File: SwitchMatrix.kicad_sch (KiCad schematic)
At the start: 134 parts, among them K1 Kailh Hotswap Socket, K10 Kailh Hotswap Socket, K11 Kailh Hotswap Socket, K12 Kailh Hotswap Socket, K13 Kailh Hotswap Socket, K14 Kailh Hotswap Socket, K15 Kailh Hotswap Socket, K16 Kailh Hotswap Socket, K17 Kailh Hotswap Socket, K18 Kailh Hotswap Socket, K19 Kailh Hotswap Socket, K2 Kailh Hotswap Socket, K20 Kailh Hotswap Socket, K21 Kailh Hotswap Socket, K22 Kailh Hotswap Socket, K23 Kailh Hotswap Socket, K24 Kailh Hotswap Socket, K25 Kailh Hotswap Socket, K26 Kailh Hotswap Socket, K27 Kailh Hotswap Socket, K28 Kailh Hotswap Socket, K29 Kailh Hotswap Socket, K3 Kailh Hotswap Socket, K30 Kailh Hotswap Socket, K31 Kailh Hotswap Socket, K32 Kailh Hotswap Socket, K33 Kailh Hotswap Socket, K34 Kailh Hotswap Socket, K35 Kailh Hotswap Socket, K36 Kailh Hotswap Socket, K37 Kailh Hotswap Socket, K38 Kailh Hotswap Socket, K39 Kailh Hotswap Socket, K4 Kailh Hotswap Socket, K40 Kailh Hotswap Socket, K41 Kailh Hotswap Socket, K42 Kailh Hotswap Socket, K43 Kailh Hotswap Socket, K44 Kailh Hotswap Socket, K45 Kailh Hotswap Socket, K46 Kailh Hotswap Socket, K47 Kailh Hotswap Socket, K48 Kailh Hotswap Socket, K49 Kailh Hotswap Socket, K5 Kailh Hotswap Socket, K50 Kailh Hotswap Socket, K51 Kailh Hotswap Socket, K52 Kailh Hotswap Socket, K53 Kailh Hotswap Socket, K54 Kailh Hotswap Socket, K55 Kailh Hotswap Socket, K56 Kailh Hotswap Socket, K57 Kailh Hotswap Socket, K58 Kailh Hotswap Socket, K59 Kailh Hotswap Socket, K6 Kailh Hotswap Socket, K60 Kailh Hotswap Socket, K61 Kailh Hotswap Socket, K62 Kailh Hotswap Socket, K63 Kailh Hotswap Socket, K64 Kailh Hotswap Socket, K7 Kailh Hotswap Socket, K8 Kailh Hotswap Socket, K9 Kailh Hotswap Socket

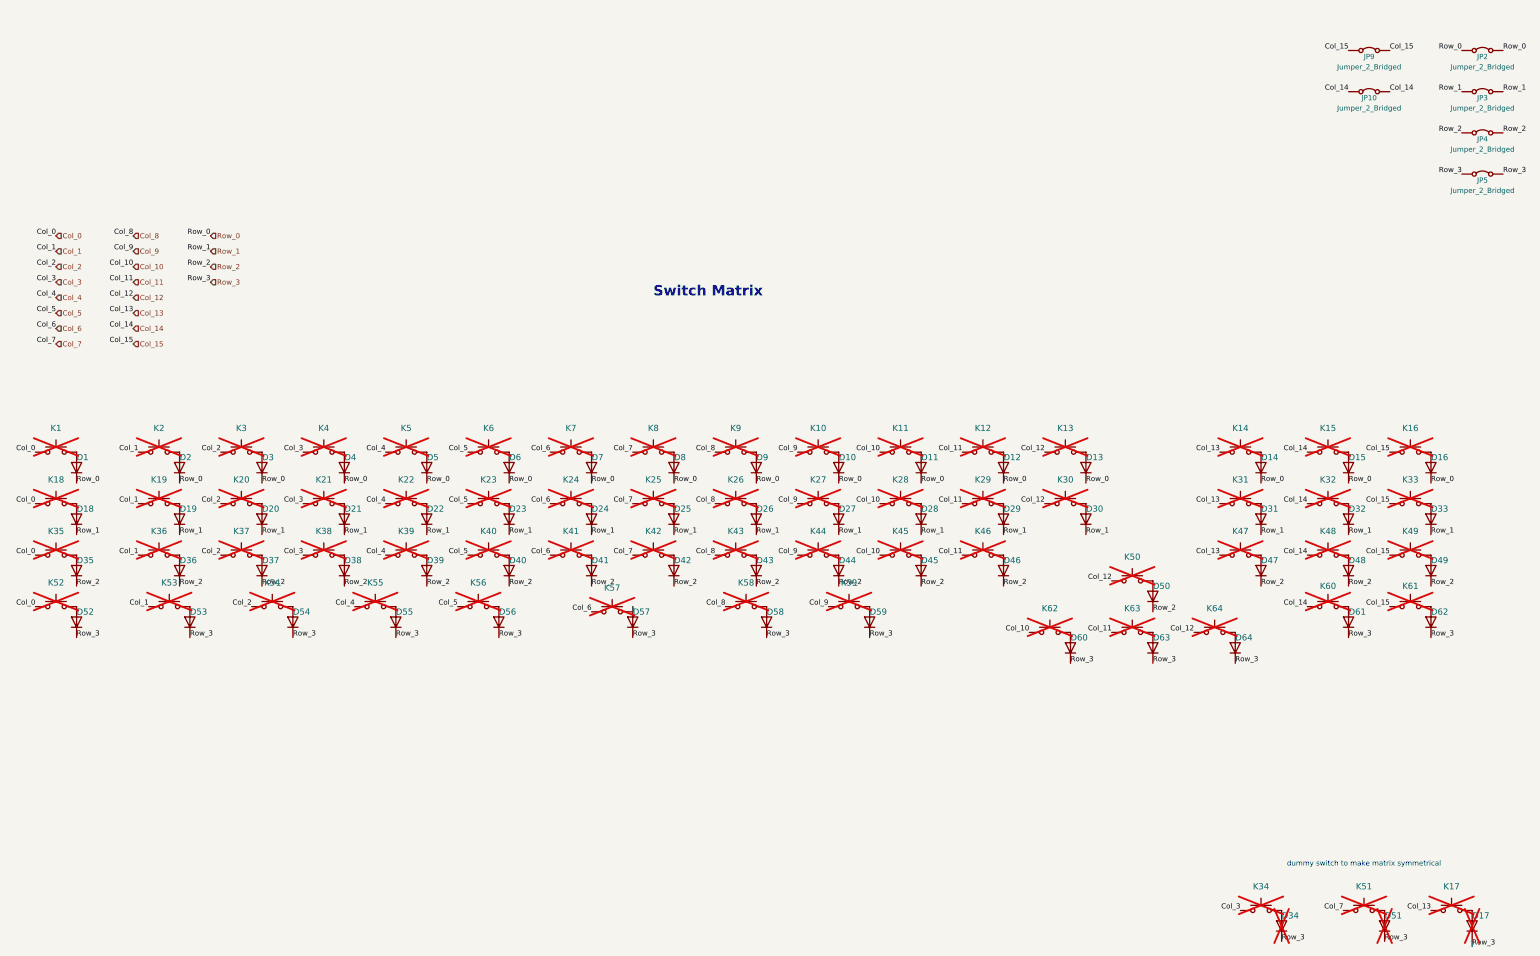
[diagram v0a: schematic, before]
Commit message: usb changes for high power (leds)
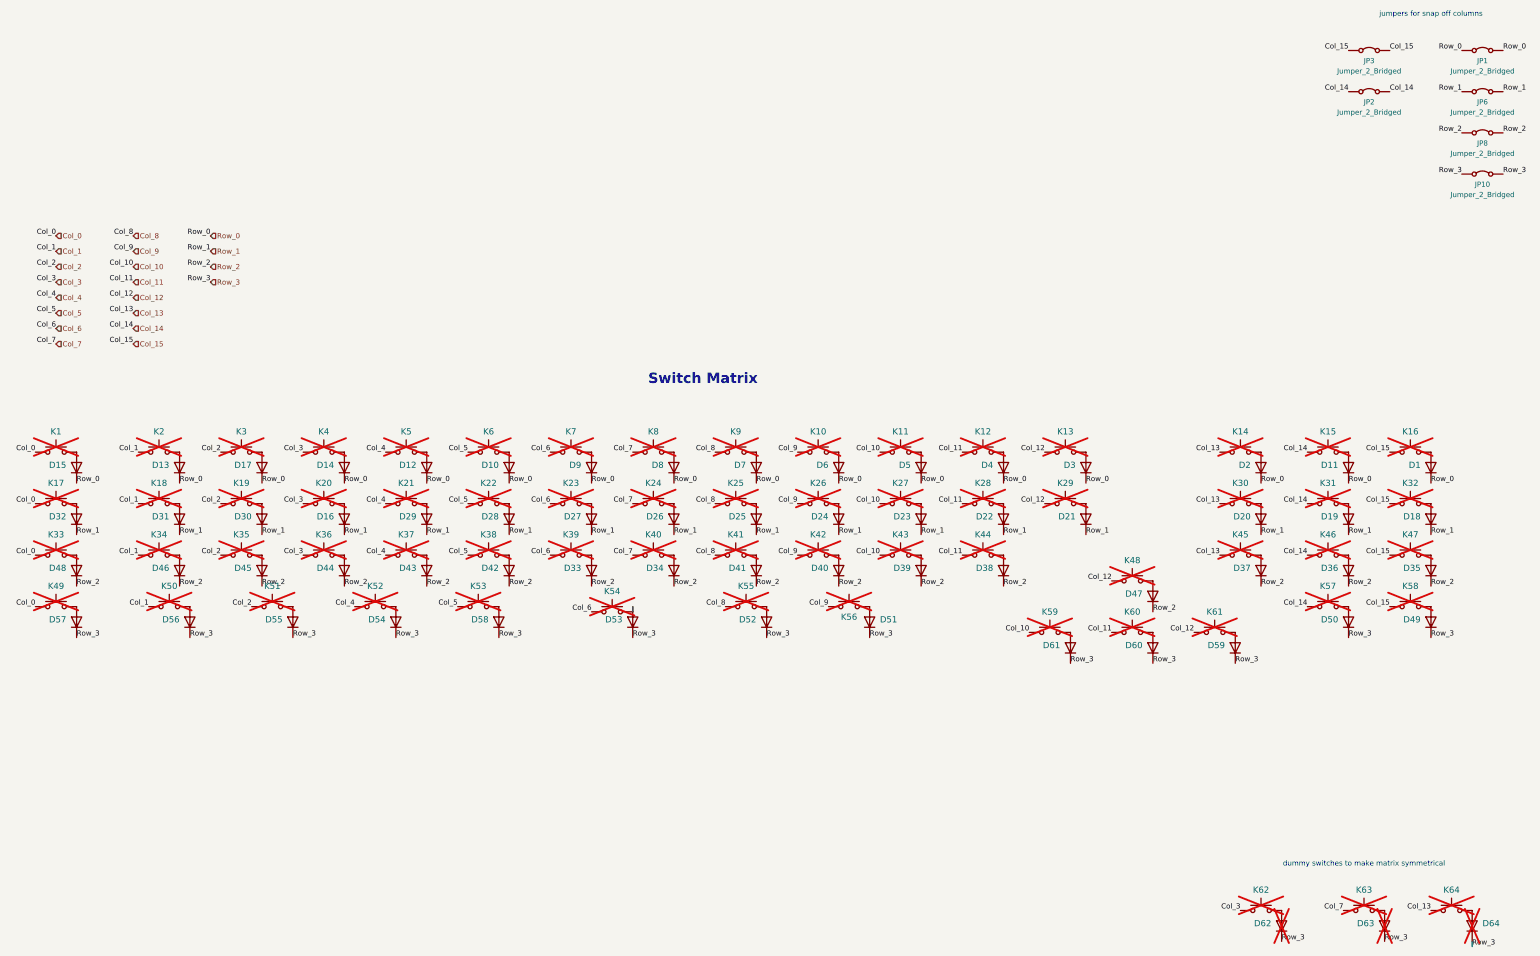
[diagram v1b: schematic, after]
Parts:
- renumbered D16 to D1, D6 to D10, D15 to D11, D5 to D12, D2 to D13, D4 to D14, D1 to D15, D21 to D16, D3 to D17, D33 to D18, D32 to D19, D14 to D2, D31 to D20, D30 to D21, D29 to D22, D28 to D23, D27 to D24, D26 to D25, D25 to D26, D24 to D27, D23 to D28, D22 to D29, D13 to D3, D20 to D30, D19 to D31, D18 to D32, D41 to D33, D42 to D34, D49 to D35, D48 to D36, D47 to D37, D46 to D38, D45 to D39, D12 to D4, D44 to D40, D43 to D41, D40 to D42, D39 to D43, D38 to D44, D37 to D45, D36 to D46, D50 to D47, D35 to D48, D62 to D49, D11 to D5, D61 to D50, D59 to D51, D58 to D52, D57 to D53, D55 to D54, D54 to D55, D53 to D56, D52 to D57, D56 to D58, D64 to D59, D10 to D6, D63 to D60, D60 to D61, D34 to D62, D51 to D63, D17 to D64, D9 to D7, D7 to D9, JP2 to JP1, JP5 to JP10, JP10 to JP2, JP9 to JP3, JP3 to JP6, JP4 to JP8, K18 to K17, K19 to K18, K20 to K19, K21 to K20, K22 to K21, K23 to K22, K24 to K23, K25 to K24, K26 to K25, K27 to K26, K28 to K27, K29 to K28, K30 to K29, K31 to K30, K32 to K31, K33 to K32, K35 to K33, K36 to K34, K37 to K35, K38 to K36, K39 to K37, K40 to K38, K41 to K39, K42 to K40, K43 to K41, K44 to K42, K45 to K43, K46 to K44, K47 to K45, K48 to K46, K49 to K47, K50 to K48, K52 to K49, K53 to K50, K54 to K51, K55 to K52, K56 to K53, K57 to K54, K58 to K55, K59 to K56, K60 to K57, K61 to K58, K62 to K59, K63 to K60, K64 to K61, K34 to K62, K51 to K63, K17 to K64
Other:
- note added: "dummy switches to make matrix symmetrical"
- note added: "jumpers for snap off columns"
- note removed: "dummy switch to make matrix symmetrical"

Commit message: bulk cap and level shifter (still need to lay out)
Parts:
- D1, D10, D11, D12, D13, D14, D15, D16, D17, D18, D19, D2, D20, D21, D22, D23, D24, D25, D26, D27, D28, D29, D3, D30, D31, D32, D33, D34, D35, D36, D37, D38, D39, D4, D40, D41, D42, D43, D44, D45, D46, D47, D48, D49, D5, D50, D51, D52, D53, D54, D55, D56, D57, D58, D59, D6, D60, D61, D7, D8, D9: LCSC C2828417 -> C81598; MPN (none) -> 1N4148W; Manufacturer 1N4148W -> ST(Semtech)
- D62, D63, D64: MPN (none) -> DNP
- JP1, JP10, JP2, JP3, JP6, JP8: MPN (none) -> DNP; now not fitted
- K1, K10, K11, K12, K13, K14, K15, K16, K17, K18, K19, K2, K20, K21, K22, K23, K24, K25, K26, K27, K28, K29, K3, K30, K31, K32, K33, K34, K35, K36, K37, K38, K39, K4, K40, K41, K42, K43, K44, K45, K46, K47, K48, K5, K57, K58, K59, K6, K60, K61, K62, K63, K64, K7, K8, K9: footprint PCM_Switch_Keyboard_Hotswap_Kailh:SW_Hotswap_Kailh_MX_1.00u -> PCM_Switch_Keyboard_Hotswap_Kailh:SW_Hotswap_Kailh_MX_Plated; MPN 4958 -> 4958
- K49, K50, K51, K52, K53, K55, K56: footprint PCM_Switch_Keyboard_Hotswap_Kailh:SW_Hotswap_Kailh_MX_1.25u -> PCM_Switch_Keyboard_Hotswap_Kailh:SW_Hotswap_Kailh_MX_Plated_1.25u; MPN 4958 -> 4958
- K54: footprint PCM_Switch_Keyboard_Hotswap_Kailh:SW_Hotswap_Kailh_MX_2.00u -> PCM_Switch_Keyboard_Hotswap_Kailh:SW_Hotswap_Kailh_MX_Plated_2.00u; MPN 4958 -> 4958

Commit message: add debug led, make bulk caps smaller, export plate and bottom for rudimentary case
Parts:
- D1, D10, D11, D12, D13, D14, D15, D16, D17, D18, D19, D2, D20, D21, D22, D23, D24, D25, D26, D27, D28, D29, D3, D30, D31, D32, D33, D34, D35, D36, D37, D38, D39, D4, D40, D41, D42, D43, D44, D45, D46, D47, D48, D49, D5, D50, D51, D52, D53, D54, D55, D56, D57, D58, D59, D6, D60, D61, D7, D8, D9: Manufacturer ST(Semtech) -> ST(Semtech)
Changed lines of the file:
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@@
 			)
 		)
-		(property "Manufacturer" " ST(Semtech)"
+		(property "Manufacturer" "ST(Semtech)"
 			(at 38.1 153.67 0)
 			(effects
@@
 			)
 		)
-		(property "Manufacturer" " ST(Semtech)"
+		(property "Manufacturer" "ST(Semtech)"
 			(at 372.11 128.27 0)
 			(effects
@@
 			)
 		)
-		(property "Manufacturer" " ST(Semtech)"
+		(property "Manufacturer" "ST(Semtech)"
 			(at 372.11 166.37 0)
 			(effects
@@
 			)
 		)
-		(property "Manufacturer" " ST(Semtech)"
+		(property "Manufacturer" "ST(Semtech)"
 			(at 233.68 166.37 0)
 			(effects
@@
 			)
 		)
-		(property "Manufacturer" " ST(Semtech)"
+		(property "Manufacturer" "ST(Semtech)"
 			(at 104.14 153.67 0)
 			(effects
@@
 			)
 		)
-		(property "Manufacturer" " ST(Semtech)"
+		(property "Manufacturer" "ST(Semtech)"
 			(at 303.53 160.02 0)
 			(effects
@@
 			)
 		)
-		(property "Manufacturer" " ST(Semtech)"
+		(property "Manufacturer" "ST(Semtech)"
 			(at 63.5 153.67 0)
 			(effects
@@
 			)
 		)
-		(property "Manufacturer" " ST(Semtech)"
+		(property "Manufacturer" "ST(Semtech)"
 			(at 104.14 140.97 0)
 			(effects
@@
 			)
 		)
-		(property "Manufacturer" " ST(Semtech)"
+		(property "Manufacturer" "ST(Semtech)"
 			(at 226.06 153.67 0)
 			(effects
@@
 			)
 		)
-		(property "Manufacturer" " ST(Semtech)"
+		(property "Manufacturer" "ST(Semtech)"
 			(at 205.74 153.67 0)
 			(effects
@@
 			)
 		)
-		(property "Manufacturer" " ST(Semtech)"
+		(property "Manufacturer" "ST(Semtech)"
 			(at 351.79 140.97 0)
 			(effects
@@
 			)
 		)
-		(property "Manufacturer" " ST(Semtech)"
+		(property "Manufacturer" "ST(Semtech)"
 			(at 124.46 140.97 0)
 			(effects
@@
 			)
 		)
-		(property "Manufacturer" " ST(Semtech)"
+		(property "Manufacturer" "ST(Semtech)"
 			(at 246.38 128.27 0)
 			(effects
@@
 			)
 		)
-		(property "Manufacturer" " ST(Semtech)"
+		(property "Manufacturer" "ST(Semtech)"
 			(at 63.5 128.27 0)
 			(effects
@@
 			)
 		)
-		(property "Manufacturer" " ST(Semtech)"
+		(property "Manufacturer" "ST(Semtech)"
 			(at 144.78 128.27 0)
 			(effects
@@
 			)
 		)
-		(property "Manufacturer" " ST(Semtech)"
+		(property "Manufacturer" "ST(Semtech)"
 			(at 83.82 140.97 0)
 			(effects
@@
 			)
 		)
-		(property "Manufacturer" " ST(Semtech)"
+		(property "Manufacturer" "ST(Semtech)"
 			(at 205.74 140.97 0)
 			(effects
@@
 			)
 		)
-		(property "Manufacturer" " ST(Semtech)"
+		(property "Manufacturer" "ST(Semtech)"
 			(at 38.1 140.97 0)
 			(effects
@@
 			)
 		)
-		(property "Manufacturer" " ST(Semtech)"
+		(property "Manufacturer" "ST(Semtech)"
 			(at 246.38 140.97 0)
 			(effects
@@
 			)
 		)
-		(property "Manufacturer" " ST(Semtech)"
+		(property "Manufacturer" "ST(Semtech)"
 			(at 124.46 128.27 0)
 			(effects
@@
 			)
 		)
-		(property "Manufacturer" " ST(Semtech)"
+		(property "Manufacturer" "ST(Semtech)"
 			(at 83.82 153.67 0)
 			(effects
@@
 			)
 		)
-		(property "Manufacturer" " ST(Semtech)"
+		(property "Manufacturer" "ST(Semtech)"
 			(at 287.02 128.27 0)
 			(effects
@@
 			)
 		)
-		(property "Manufacturer" " ST(Semtech)"
+		(property "Manufacturer" "ST(Semtech)"
 			(at 66.04 166.37 0)
 			(effects
@@
 			)
 		)
-		(property "Manufacturer" " ST(Semtech)"
+		(property "Manufacturer" "ST(Semtech)"
 			(at 185.42 128.27 0)
 			(effects
@@
 			)
 		)
-		(property "Manufacturer" " ST(Semtech)"
+		(property "Manufacturer" "ST(Semtech)"
 			(at 175.26 166.37 0)
 			(effects
@@
 			)
 		)
-		(property "Manufacturer" " ST(Semtech)"
+		(property "Manufacturer" "ST(Semtech)"
 			(at 116.84 166.37 0)
 			(effects
@@
 			)
 		)
-		(property "Manufacturer" " ST(Semtech)"
+		(property "Manufacturer" "ST(Semtech)"
 			(at 165.1 153.67 0)
 			(effects
@@
 			)
 		)
-		(property "Manufacturer" " ST(Semtech)"
+		(property "Manufacturer" "ST(Semtech)"
 			(at 226.06 140.97 0)
 			(effects
@@
 			)
 		)
-		(property "Manufacturer" " ST(Semtech)"
+		(property "Manufacturer" "ST(Semtech)"
 			(at 91.44 166.37 0)
 			(effects
@@
 			)
 		)
-		(property "Manufacturer" " ST(Semtech)"
+		(property "Manufacturer" "ST(Semtech)"
 			(at 372.11 153.67 0)
 			(effects
@@
 			)
 		)
-		(property "Manufacturer" " ST(Semtech)"
+		(property "Manufacturer" "ST(Semtech)"
 			(at 104.14 128.27 0)
 			(effects
@@
 			)
 		)
-		(property "Manufacturer" " ST(Semtech)"
+		(property "Manufacturer" "ST(Semtech)"
 			(at 351.79 153.67 0)
 			(effects
@@
 			)
 		)
-		(property "Manufacturer" " ST(Semtech)"
+		(property "Manufacturer" "ST(Semtech)"
 			(at 144.78 140.97 0)
 			(effects
@@
 			)
 		)
-		(property "Manufacturer" " ST(Semtech)"
+		(property "Manufacturer" "ST(Semtech)"
 			(at 165.1 128.27 0)
 			(effects
@@
 			)
 		)
-		(property "Manufacturer" " ST(Semtech)"
+		(property "Manufacturer" "ST(Semtech)"
 			(at 208.28 166.37 0)
 			(effects
@@
 			)
 		)
-		(property "Manufacturer" " ST(Semtech)"
+		(property "Manufacturer" "ST(Semtech)"
 			(at 246.38 153.67 0)
 			(effects
@@
 			)
 		)
-		(property "Manufacturer" " ST(Semtech)"
+		(property "Manufacturer" "ST(Semtech)"
 			(at 266.7 140.97 0)
 			(effects
@@
 			)
 		)
-		(property "Manufacturer" " ST(Semtech)"
+		(property "Manufacturer" "ST(Semtech)"
 			(at 330.2 128.27 0)
 			(effects
@@
 			)
 		)
-		(property "Manufacturer" " ST(Semtech)"
+		(property "Manufacturer" "ST(Semtech)"
 			(at 205.74 128.27 0)
 			(effects
@@
 			)
 		)
-		(property "Manufacturer" " ST(Semtech)"
+		(property "Manufacturer" "ST(Semtech)"
 			(at 287.02 140.97 0)
 			(effects
@@
 			)
 		)
-		(property "Manufacturer" " ST(Semtech)"
+		(property "Manufacturer" "ST(Semtech)"
 			(at 38.1 128.27 0)
 			(effects
@@
 			)
 		)
-		(property "Manufacturer" " ST(Semtech)"
+		(property "Manufacturer" "ST(Semtech)"
 			(at 283.21 172.72 0)
 			(effects
@@
 			)
 		)
-		(property "Manufacturer" " ST(Semtech)"
+		(property "Manufacturer" "ST(Semtech)"
 			(at 266.7 128.27 0)
 			(effects
@@
 			)
 		)
-		(property "Manufacturer" " ST(Semtech)"
+		(property "Manufacturer" "ST(Semtech)"
 			(at 303.53 172.72 0)
 			(effects
@@
 			)
 		)
-		(property "Manufacturer" " ST(Semtech)"
+		(property "Manufacturer" "ST(Semtech)"
 			(at 63.5 140.97 0)
 			(effects
@@
 			)
 		)
-		(property "Manufacturer" " ST(Semtech)"
+		(property "Manufacturer" "ST(Semtech)"
 			(at 226.06 128.27 0)
 			(effects
@@
 			)
 		)
-		(property "Manufacturer" " ST(Semtech)"
+		(property "Manufacturer" "ST(Semtech)"
 			(at 351.79 128.27 0)
 			(effects
@@
 			)
 		)
-		(property "Manufacturer" " ST(Semtech)"
+		(property "Manufacturer" "ST(Semtech)"
 			(at 330.2 140.97 0)
 			(effects
@@
 			)
 		)
-		(property "Manufacturer" " ST(Semtech)"
+		(property "Manufacturer" "ST(Semtech)"
 			(at 330.2 153.67 0)
 			(effects
@@
 			)
 		)
-		(property "Manufacturer" " ST(Semtech)"
+		(property "Manufacturer" "ST(Semtech)"
 			(at 38.1 166.37 0)
 			(effects
@@
 			)
 		)
-		(property "Manufacturer" " ST(Semtech)"
+		(property "Manufacturer" "ST(Semtech)"
 			(at 144.78 153.67 0)
 			(effects
@@
 			)
 		)
-		(property "Manufacturer" " ST(Semtech)"
+		(property "Manufacturer" "ST(Semtech)"
 			(at 185.42 153.67 0)
 			(effects
@@
 			)
 		)
-		(property "Manufacturer" " ST(Semtech)"
+		(property "Manufacturer" "ST(Semtech)"
 			(at 372.11 140.97 0)
 			(effects
@@
 			)
 		)
-		(property "Manufacturer" " ST(Semtech)"
+		(property "Manufacturer" "ST(Semtech)"
 			(at 124.46 153.67 0)
 			(effects
@@
 			)
 		)
-		(property "Manufacturer" " ST(Semtech)"
+		(property "Manufacturer" "ST(Semtech)"
 			(at 266.7 153.67 0)
 			(effects
@@
 			)
 		)
-		(property "Manufacturer" " ST(Semtech)"
+		(property "Manufacturer" "ST(Semtech)"
 			(at 351.79 166.37 0)
 			(effects
@@
 			)
 		)
-		(property "Manufacturer" " ST(Semtech)"
+		(property "Manufacturer" "ST(Semtech)"
 			(at 142.24 166.37 0)
 			(effects
@@
 			)
 		)
-		(property "Manufacturer" " ST(Semtech)"
+		(property "Manufacturer" "ST(Semtech)"
 			(at 83.82 128.27 0)
 			(effects
@@
 			)
 		)
-		(property "Manufacturer" " ST(Semtech)"
+		(property "Manufacturer" "ST(Semtech)"
 			(at 185.42 140.97 0)
 			(effects
@@
 			)
 		)
-		(property "Manufacturer" " ST(Semtech)"
+		(property "Manufacturer" "ST(Semtech)"
 			(at 165.1 140.97 0)
 			(effects
@@
 			)
 		)
-		(property "Manufacturer" " ST(Semtech)"
+		(property "Manufacturer" "ST(Semtech)"
 			(at 323.85 172.72 0)
 			(effects

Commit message: enlarge mounting holes, custom rules
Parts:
- JP1, JP10, JP2, JP3, JP6, JP8: value Jumper_2_Bridged -> Jumper_2_Small_Bridged; symbol Jumper:Jumper_2_Bridged -> Jumper:Jumper_2_Small_Bridged; now in the parts list
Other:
- moved on the sheet: D1, D10, D11, D12, D13, D14, D15, D16, D17, D18, D19, D2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

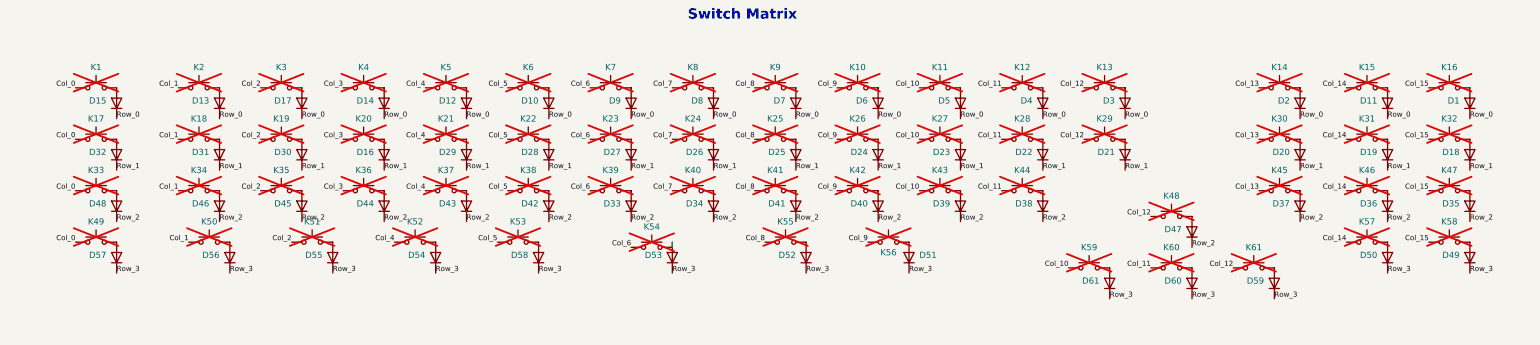
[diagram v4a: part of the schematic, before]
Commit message: fab output changes (part choice updates)
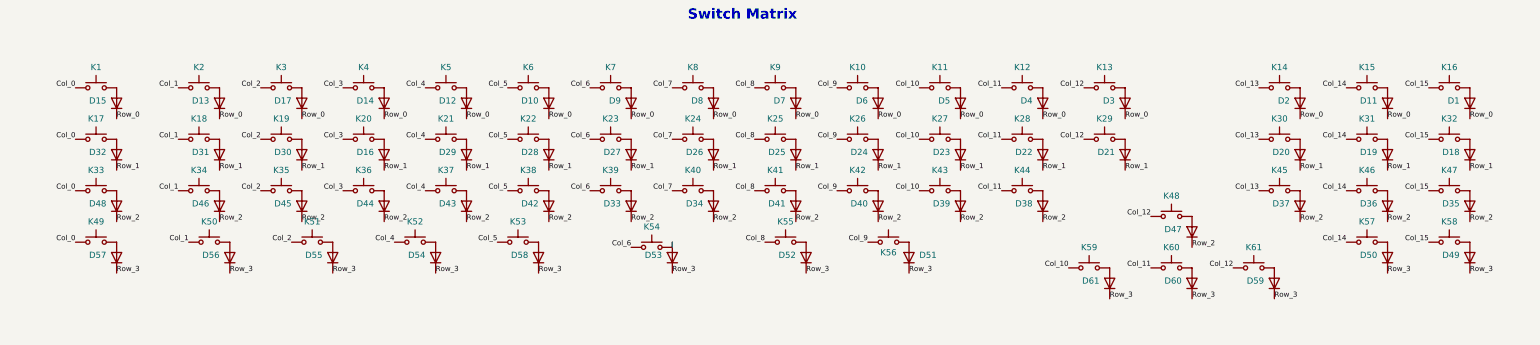
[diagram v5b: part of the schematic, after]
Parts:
- D62, D63, D64: Type DNS -> SMD
- JP1, JP10, JP2, JP3, JP6, JP8: now left out of the parts list
- K1, K10, K11, K12, K13, K14, K15, K16, K17, K18, K19, K2, K20, K21, K22, K23, K24, K25, K26, K27, K28, K29, K3, K30, K31, K32, K33, K34, K35, K36, K37, K38, K39, K4, K40, K41, K42, K43, K44, K45, K46, K47, K48, K5, K57, K58, K59, K6, K60, K61, K7, K8, K9: footprint PCM_Switch_Keyboard_Hotswap_Kailh:SW_Hotswap_Kailh_MX_Plated -> PCM_Switch_Keyboard_Hotswap_Kailh:SW_Hotswap_Kailh_MX_1.00u; LCSC (none) -> C5156480; now fitted
- K49, K50, K51, K52, K53, K55, K56: footprint PCM_Switch_Keyboard_Hotswap_Kailh:SW_Hotswap_Kailh_MX_Plated_1.25u -> PCM_Switch_Keyboard_Hotswap_Kailh:SW_Hotswap_Kailh_MX_1.00u; LCSC (none) -> C5156480; now fitted
- K54: footprint PCM_Switch_Keyboard_Hotswap_Kailh:SW_Hotswap_Kailh_MX_Plated_2.00u -> PCM_Switch_Keyboard_Hotswap_Kailh:SW_Hotswap_Kailh_MX_1.00u; LCSC (none) -> C5156480; now fitted
- K62, K63, K64: LCSC (none) -> C2803348

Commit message: switch to solderable sockets, you can millmax if you want.
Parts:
- K1, K10, K11, K12, K13, K14, K15, K16, K17, K18, K19, K2, K20, K21, K22, K23, K24, K25, K26, K27, K28, K29, K3, K30, K31, K32, K33, K34, K35, K36, K37, K38, K39, K4, K40, K41, K42, K43, K44, K45, K46, K47, K48, K49, K5, K50, K51, K52, K53, K54, K55, K56, K57, K58, K59, K6, K60, K61, K7, K8, K9: footprint PCM_Switch_Keyboard_Hotswap_Kailh:SW_Hotswap_Kailh_MX_1.00u -> PCM_Switch_Keyboard_Cherry_MX:SW_Cherry_MX_PCB_1.00u
- K62, K63, K64: footprint PCM_Switch_Keyboard_Hotswap_Kailh:SW_Hotswap_Kailh_MX_Plated -> PCM_Switch_Keyboard_Cherry_MX:SW_Cherry_MX_PCB_1.00u
